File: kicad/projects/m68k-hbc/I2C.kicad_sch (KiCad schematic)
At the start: 2 parts, among them U10 PCA9564, U11 PCA9541D

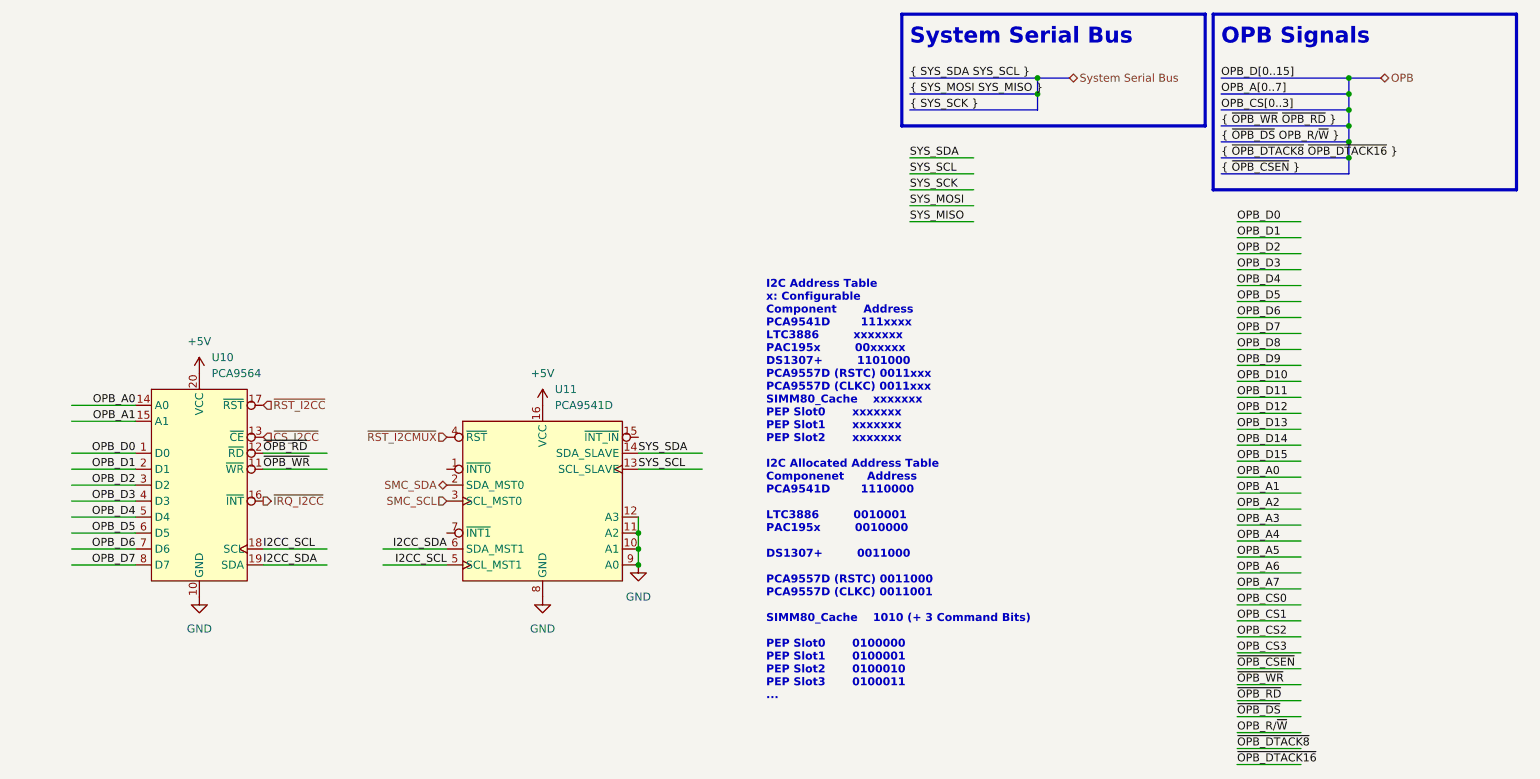
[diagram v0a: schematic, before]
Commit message: Large changes: EHBCSimpleEmu, kicad, fwcode, docs
This commit contains some large changes:
- Removed EHBCSimpleEmu (Moved to kms1212/llemu, kms1212/qemu)
- (likely) Removed fwcode; now it only boots and stops
- Modified documents
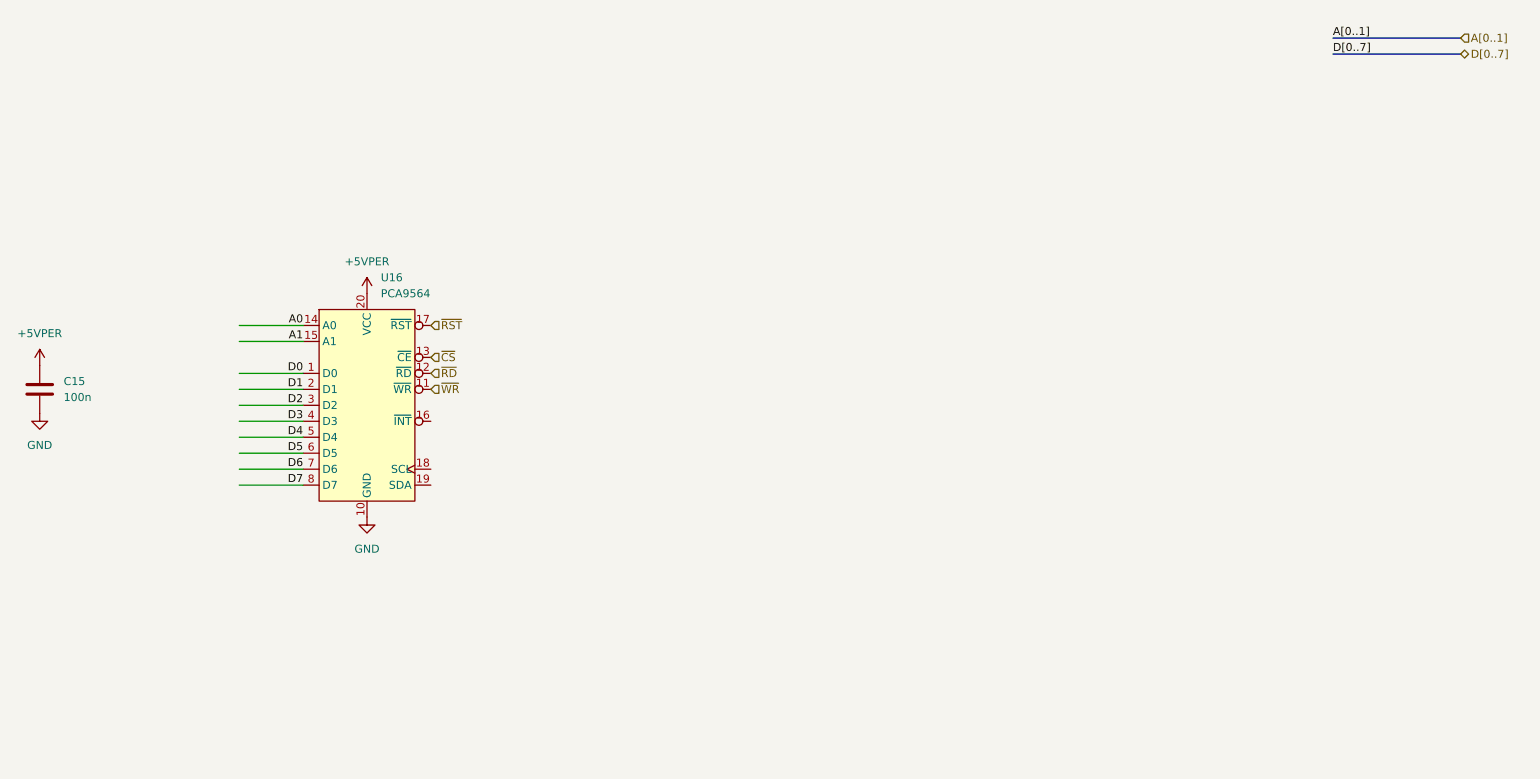
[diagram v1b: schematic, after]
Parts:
- removed U10: PCA9564, Package_SO:TSSOP-20_4.4x6.5mm_P0.65mm, symbol m68k-hbc-ic:PCA9564
- removed U11: PCA9541D, Package_SO:SO-16_3.9x9.9mm_P1.27mm, symbol m68k-hbc-ic:PCA9541D
- added C15: 100n, Capacitor_THT:C_Disc_D6.0mm_W2.5mm_P5.00mm, symbol Device:C
- added U16: PCA9564, Package_SO:TSSOP-20_4.4x6.5mm_P0.65mm, symbol m68k-hbc-ic:PCA9564
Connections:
- net GND: now also C15.2, U16.10 (GND)
- new net +5VPER: C15.1, U16.20 (VCC)
- new net A0: U16.14 (A0)
- new net A1: U16.15 (A1)
- new net D0: U16.1 (D0)
- new net D1: U16.2 (D1)
- new net D2: U16.3 (D2)
- new net D3: U16.4 (D3)
- new net D4: U16.5 (D4)
- new net D5: U16.6 (D5)
- new net D6: U16.7 (D6)
- new net D7: U16.8 (D7)
- new net ~{CS}: U16.13 (~{CE})
- new net ~{RD}: U16.12 (~{RD})
- new net ~{RST}: U16.17 (~{RST})
- new net ~{WR}: U16.11 (~{WR})
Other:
- note removed: "I2C Address Table x: Configurable Component Address PCA9541D 111xxxx LTC3886 xxxxxxx PAC195x 00xxxxx DS1307+ 1101000 PCA9557D (RSTC) 0011xxx PCA9557D (CLKC) 0011xxx SIMM80_Cache xxxxxxx PEP Slot0 xxxxxxx PEP Slot1 xxxxxxx PEP Slot2 xxxxxxx I2C Allocated Address Table Componenet Address PCA9541D 1110000 LTC3886 0010001 PAC195x 0010000 DS1307+ 0011000 PCA9557D (RSTC) 0011000 PCA9557D (CLKC) 0011001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"
- note removed: "OPB Signals"
- note removed: "System Serial Bus"
